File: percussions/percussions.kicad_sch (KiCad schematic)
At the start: 35 parts, among them J1 Conn_01x10, Q2 BC547, Q3 BC547, Q4 BC547, Q5 BC547, SW1 E-SWITCH-SW_Push_LED, SW2 E-SWITCH-SW_Push_LED, SW3 E-SWITCH-SW_Push_LED, SW4 E-SWITCH-SW_Push_LED, U1 74HC14

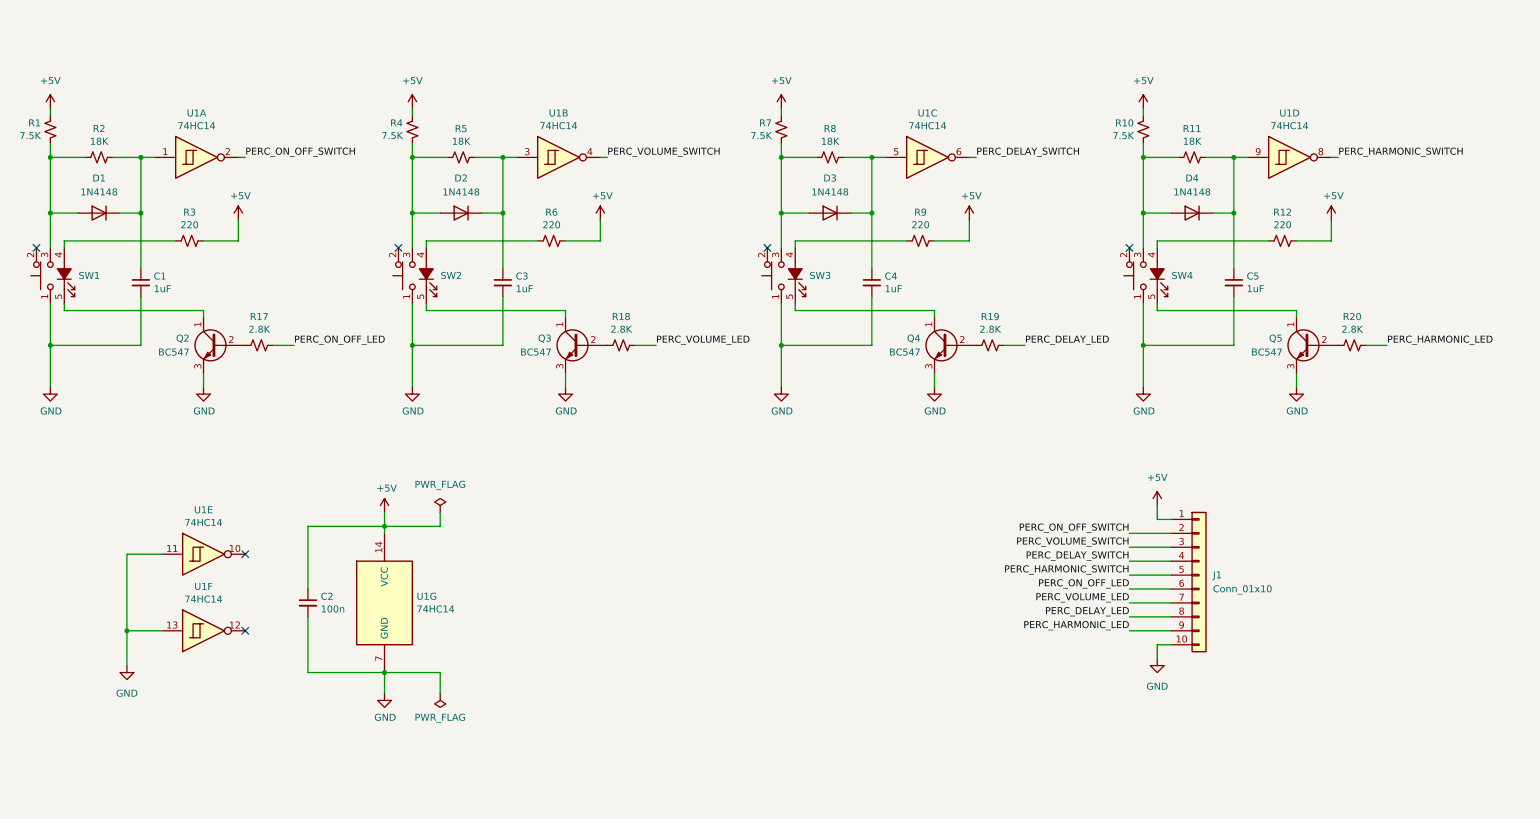
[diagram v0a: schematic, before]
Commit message: New organ architecture with mother board
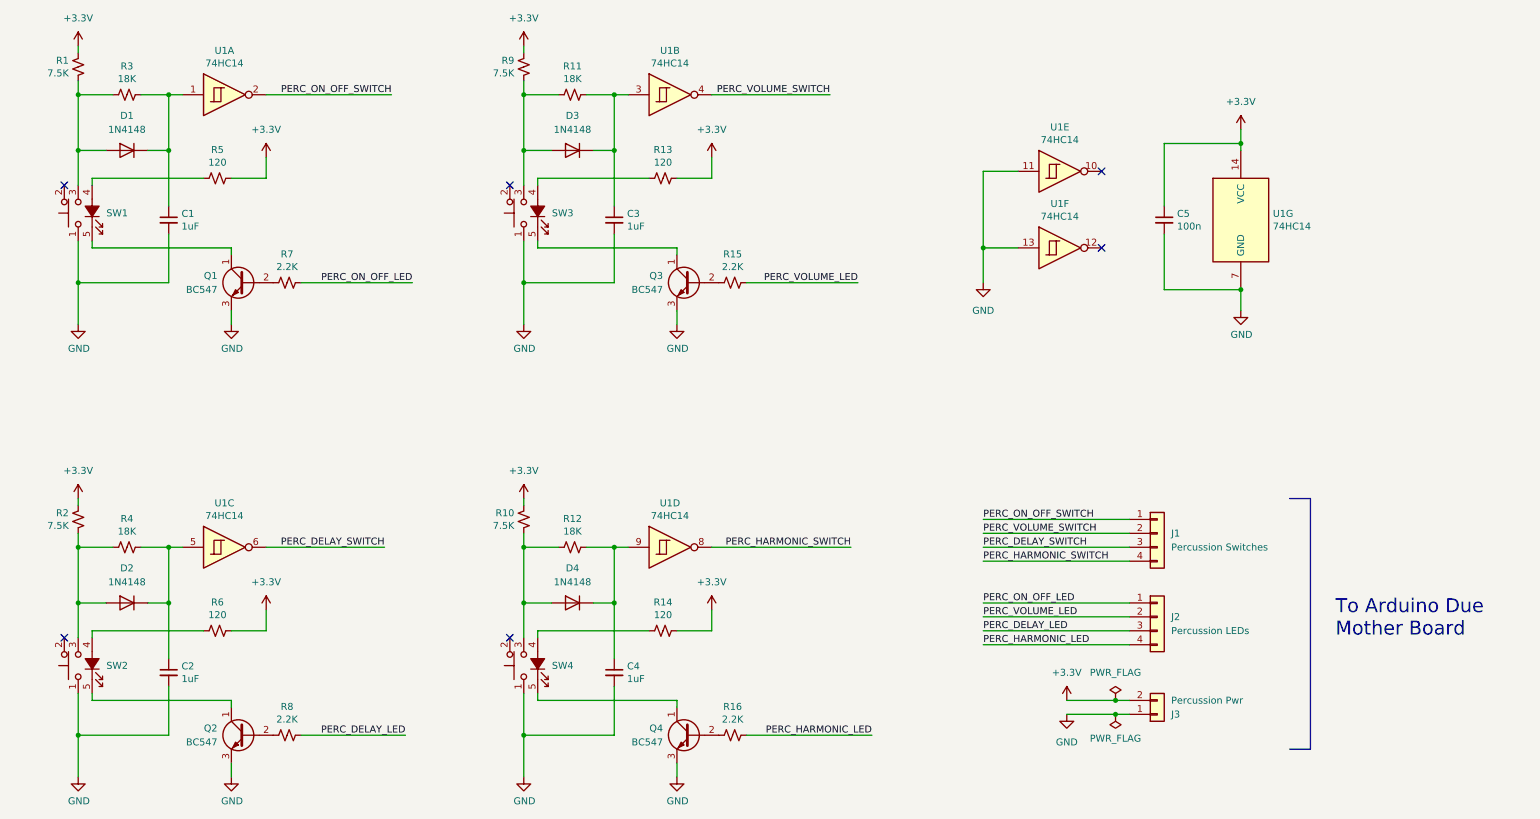
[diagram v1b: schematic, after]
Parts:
- removed J1: Conn_01x10, symbol Connector_Generic:Conn_01x10
- added J1: Percussion Switches, Connector_JST:JST_XH_B4B-XH-A_1x04_P2.50mm_Vertical, symbol Connector_Generic:Conn_01x04
- added J2: Percussion LEDs, Connector_JST:JST_XH_B4B-XH-A_1x04_P2.50mm_Vertical, symbol Connector_Generic:Conn_01x04
- added J3: Percussion Pwr, Connector_JST:JST_XH_B2B-XH-A_1x02_P2.50mm_Vertical, symbol Connector_Generic:Conn_01x02
- R13: renamed from R6; value 220 -> 120
- R14: renamed from R12; value 220 -> 120
- R15: renamed from R18; value 2.8K -> 2.2K
- R16: renamed from R20; value 2.8K -> 2.2K
- R5: renamed from R3; value 220 -> 120
- R6: renamed from R9; value 220 -> 120
- R7: renamed from R17; value 2.8K -> 2.2K
- R8: renamed from R19; value 2.8K -> 2.2K
- SW1, SW4: footprint b3_buttons_library:5511MBLKRED -> b3_footprints:5511MBLKRED
- SW2: renamed from SW3; footprint b3_buttons_library:5511MBLKRED -> b3_footprints:5511MBLKRED
- SW3: renamed from SW2; footprint b3_buttons_library:5511MBLKRED -> b3_footprints:5511MBLKRED
- U1: footprint Package_SO:SOIC-14_3.9x8.7mm_P1.27mm -> Package_DIP:DIP-14_W7.62mm_LongPads
- renumbered C4 to C2, C5 to C4, C2 to C5, D3 to D2, D2 to D3, Q2 to Q1, Q4 to Q2, Q5 to Q4, R5 to R11, R11 to R12, R7 to R2, R2 to R3, R8 to R4, R4 to R9
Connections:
- net GND: now also J3.1 (Pin_1)
- net PERC_DELAY_LED: now also J2.3 (Pin_3)
- net PERC_DELAY_SWITCH: now also J1.3 (Pin_3)
- net PERC_HARMONIC_LED: now also J2.4 (Pin_4)
- net PERC_HARMONIC_SWITCH: now also J1.4 (Pin_4)
- net PERC_ON_OFF_LED: now also J2.1 (Pin_1)
- net PERC_ON_OFF_SWITCH: now also J1.1 (Pin_1)
- net PERC_VOLUME_LED: now also J2.2 (Pin_2)
- net PERC_VOLUME_SWITCH: now also J1.2 (Pin_2)
- net +5V renamed +3.3V
- net +3.3V: now also J3.2 (Pin_2)
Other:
- note added: "To Arduino Due Mother Board"
- moved on the sheet: C1, C2, C3, C4, C5, D1, D2, D3, D4, Q1, Q2, Q3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
